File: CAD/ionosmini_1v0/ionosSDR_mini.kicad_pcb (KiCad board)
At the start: 4 copper layers, 168 x 80 mm, 63 parts, among them CON1 TFC-120-02-F-D-A-K-TR, CON2 TFC-120-02-F-D-A-K-TR, IC1 ESP32-S3-DEVKITC-1-N8R2, SW1 PTS647SK38SMTR2 LFS, SW2 PTS647SK38SMTR2 LFS, SW3 PTS647SK38SMTR2 LFS, SW4 PTS647SK38SMTR2 LFS, SW5 BACK, SW6 OK, U1 LP5907MFX-3.3

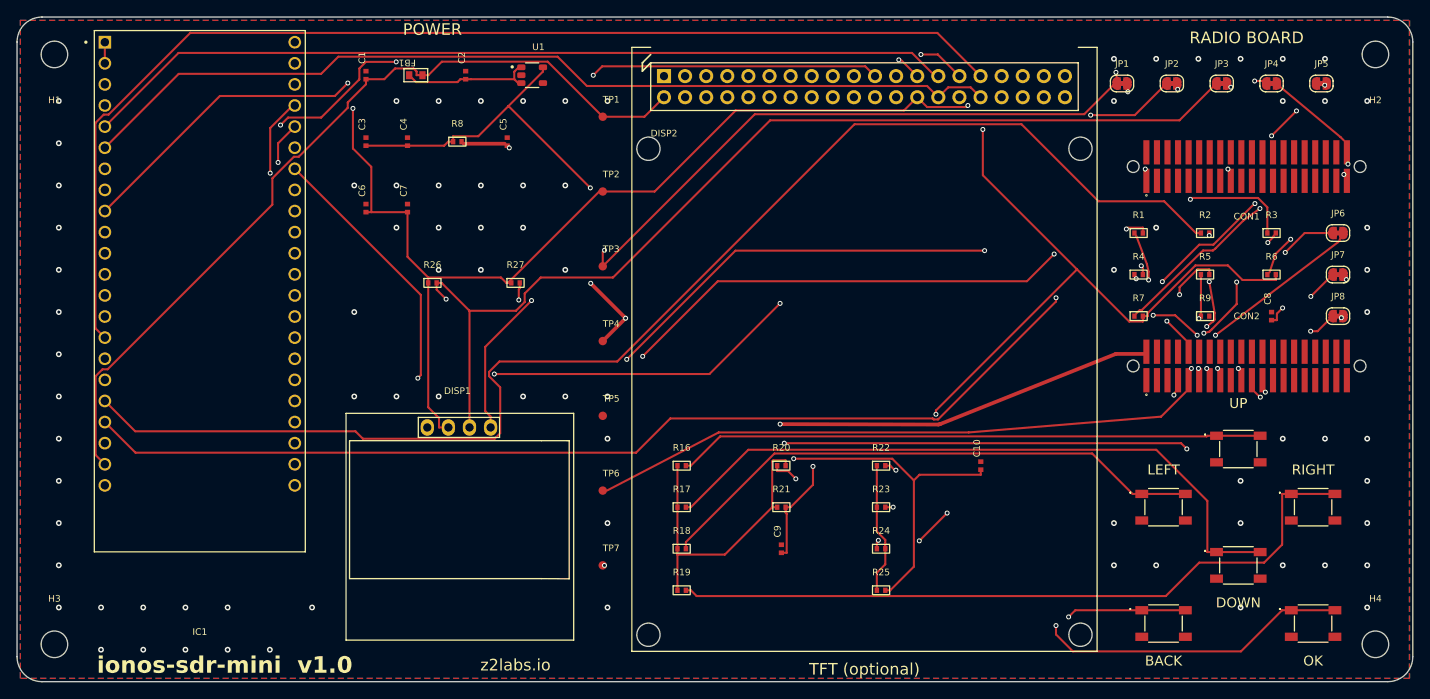
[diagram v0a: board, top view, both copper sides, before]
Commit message: layout: rev-B, routed to the Olimex house style
Measured four Olimex OLinuXino boards (A64 rev H, STMP157-LIME2 rev B1,
LCD-DRIVER rev D, LCD-15.6FHD rev H) and compared our rev-A against them.
Five differences were real; one was in our favour.

  45 degree grid   they run 99.4-100 % of segments on it, we ran 90.8 %.
                   The any-angle segments came from the autorouter's
                   pull-tight smoothing, which rev-B turns off: 100.00 %.
  width ladder     they use 8-24 widths keyed to function, we used two
                   (0.25 and 0.45).  rev-B has six netclasses -
                   0.20 Slow / 0.25 Default+SPI / 0.30 I2C / 0.40 Supply_RB
                   / 0.50 Power / 0.60 Power_HC.
  via ladder       sized per class, 0.60/0.30 and 0.70/0.35, drills restored
                   after the session import (KiCad forces them to the default).
  mask relief      every Olimex board sets pad_to_mask_clearance 0.051 mm;
                   ours was 0.  Now 0.051.
  silk weight      their reference text is ~0.25 x its height; ours was
                   0.13 mm on 0.8 mm, under the usual 0.15 mm fab floor.
                   Now 0.20 mm.
  courtyards       here we are ahead: Olimex ships 455 of 459 footprints
                   with no courtyard, we are at 12 of 63.  Left alone.

Two things the Olimex numbers could NOT be copied straight:

  clearance   their classes all share one clearance (A64 0.107 mm, STMP157
              0.127 mm) - they differentiate width, never clearance.  A first
              attempt at 0.30 mm on Power_HC was unbuildable: U1 is SOT-23-5
              with 0.25 mm between its own pads, so the footprint violated
              the rule.  All classes now sit at the board clearance, 0.20 mm.
  width cap   1.0 mm power tracks (right for a Linux SBC pulling amps) wrapped
              around U1 and sealed its GND pad into a 1.12 x 0.64 mm pocket of
              top-layer pour, too small for any legal via - the LDO ground had
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
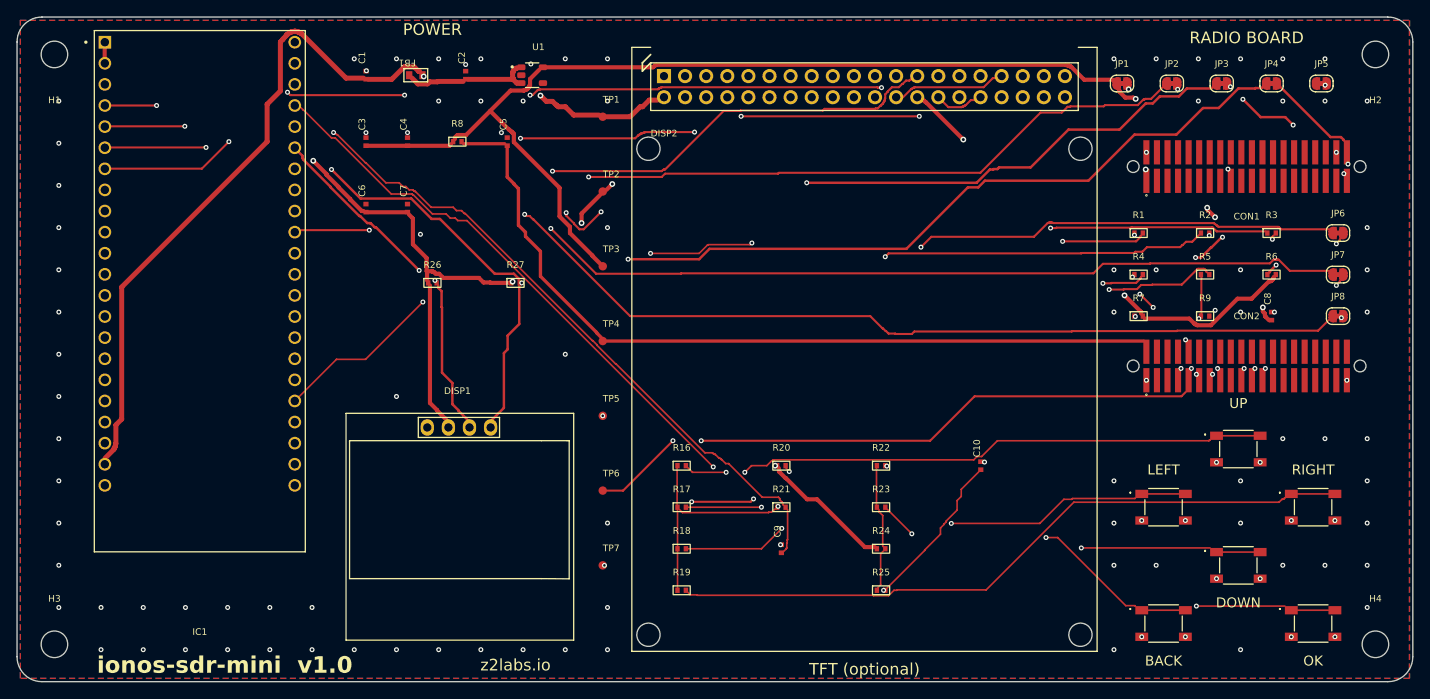
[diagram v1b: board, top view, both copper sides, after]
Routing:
- net Net-(IC1-GPIO14): track 182.3 -> 140.8 mm
- net 3V3: track 277.2 -> 247.9 mm, vias 6 -> 7
- net BTN_A: track 137.0 -> 112.8 mm
- net FG23_SCLK: track 161.1 -> 139.1 mm, vias 0 -> 1
- net TCH_B: track 139.5 -> 118.3 mm
- net SWDIO: track 147.9 -> 127.4 mm, vias 3 -> 2
- net I2C_SDA: track 167.1 -> 148.3 mm, vias 4 -> 3
- net BTN_B: track 100.8 -> 82.3 mm, vias 2 -> 1
- net TCH_A: track 126.4 -> 110.0 mm
- net TFT_BL: track 127.4 -> 111.4 mm, vias 1 -> 2
- net RESETn: track 122.1 -> 108.8 mm
- net SWCLK: track 142.8 -> 130.5 mm
- net BTN_B2: track 80.7 -> 68.6 mm, vias 0 -> 2
- net FG23_MOSI: track 142.7 -> 131.2 mm
- net 3V3_RADIO: track 162.4 -> 152.4 mm
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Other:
- rule pad_to_mask_clearance: 0 -> 0.051

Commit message: layout: rev-B2 - new front-panel placement, full re-route
Placement (agreed from a 1:1 graphical trial before touching the board):
  * small OLED (DISP1) moved up, its top edge on one line with the TFT
    (y = 53.6 mm); its I2C header now sits next to the DevKit's J3_6/J3_7
  * power block (U1, C1-C7, FB1, R8) 31 mm down into the OLED's old place.
    The placement-time estimate said 3V3_RADIO would get ~27 mm longer; the
    routed copper says otherwise - twin layer 3 measures 3V3_RADIO+VMCU_IN
    at 234 mm (rev-B 260 mm), 23.4 mV IR drop at 50 mA (rev-B 26.0 mV)
  * BACK / OK to the left of the TFT at (95,112) / (111,112), the same
    height as the centre of the cursor cross, which stays on the right and
    moves 3 mm down to clear the radio board
  * DISP1 finally has a courtyard and fab outline, drawn from its module
    silkscreen (27.4 x 27.3 mm), identically in the library and on the
    instance - layer 4 of the twin no longer fails on it

Routing - applies routing literature (Yan-Ma-Wong 2012, PCBWorld 2026,
Tang et al. 2020 survey, Gandhi 2024):
  * two passes.  Pass 1 routes only the fast buses (FG23 SPI to the
    mezzanine, TFT SPI, touch) with F.Cu demoted to an expensive layer, so
    they run on In2, the stripline between the two GND planes, and use F.Cu
    only to escape and to cross.  That is Yan-Ma-Wong's per-bus layer
    assignment done by negotiation, plus their "vias at the ends only".
    Pass 2 routes everything else with the first pass's copper fixed.
  * scored with the PCBWorld objective, Phi = -(f_drv + 0.002 WL + 0.1 vias),
    plus our own RF metrics, against the single-pass rev-B recipe on the
    same placement:
                            single pass    two-pass (chosen)
      fast-bus copper on In2   71.7 %         99.2 %
      mid-route vias, fast     29             16
      wirelength               4209 mm        4243 mm (+0.8 %)
      routing vias             103            110
    the single pass is marginally better on Ph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
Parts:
- moved SW6 95.6 mm to (111.0, 112.0)
- moved SW5 93.6 mm to (95.0, 112.0)
- moved DISP1 44.0 mm to (103.0, 66.0)
- moved C1 31.0 mm to (92.0, 88.0)
- moved C2 31.0 mm to (104.0, 88.0)
- moved C3 31.0 mm to (92.0, 96.0)
- moved C4 31.0 mm to (97.0, 96.0)
- moved C5 31.0 mm to (109.0, 96.0)
- moved C6 31.0 mm to (92.0, 104.0)
- moved C7 31.0 mm to (97.0, 104.0)
- moved FB1 31.0 mm to (98.0, 88.0)
- moved R8 31.0 mm to (103.0, 96.0)
- moved U1 31.0 mm to (112.0, 88.0)
- moved SW1 3.00 mm to (197.0, 105.0)
- moved SW2 3.00 mm to (197.0, 119.0)
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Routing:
- net 3V3: track 247.9 -> 273.3 mm, vias 7 -> 10
- net BTN_A1: track 40.6 -> 62.0 mm
- net VMCU_IN: track 97.0 -> 83.8 mm, vias 0 -> 2
- net 3V3_RADIO: track 152.4 -> 139.3 mm, vias 4 -> 10
- net 5V0: track 108.7 -> 96.1 mm, vias 2 -> 4
- net BTN_A2: track 56.4 -> 44.0 mm
- net TFT_MOSI: track 111.5 -> 120.4 mm
- net TFT_SCK: track 107.3 -> 114.8 mm, vias 5 -> 2
- net TFT_MISO: track 105.6 -> 109.9 mm, vias 5 -> 1
- net I2C_SCL: track 144.7 -> 140.5 mm, vias 3 -> 2
- net FG23_SPARE_RB: track 41.4 -> 45.0 mm
- net TFT_TE: track 98.9 -> 102.3 mm, vias 0 -> 2
- net BTN_B3: track 60.1 -> 63.4 mm, vias 2 -> 0
- net SWO: track 130.8 -> 134.0 mm, vias 1 -> 2
- net TFT_RST: track 99.0 -> 102.1 mm, vias 0 -> 1
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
